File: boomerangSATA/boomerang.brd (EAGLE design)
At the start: 84.1 x 79.3 mm, 12 parts

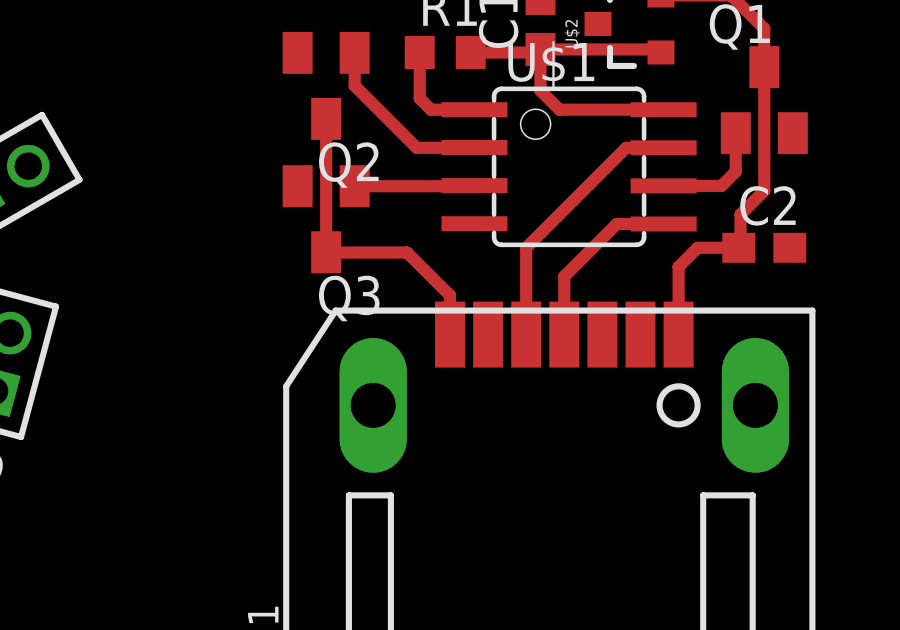
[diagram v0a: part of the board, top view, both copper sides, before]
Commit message: updated SATA - connector part in library used
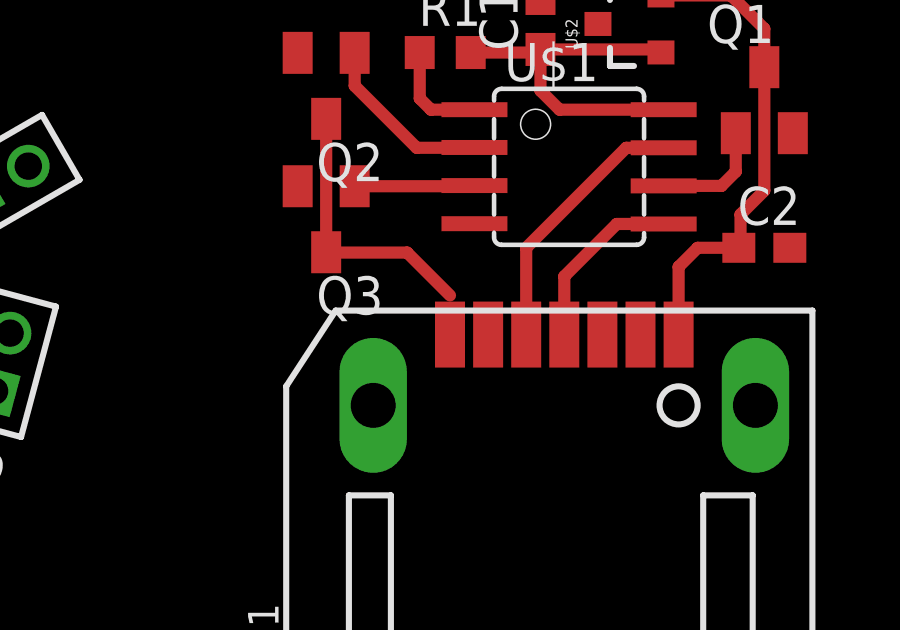
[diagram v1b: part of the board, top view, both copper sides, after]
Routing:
- net VCC: track 26.6 -> 25.3 mm
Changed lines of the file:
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@@
 <param name="tpViaShape" value="round"/>
 <param name="PrefDir.1" value="|"/>
-<param name="PrefDir.2" value="-"/>
-<param name="PrefDir.3" value="-"/>
-<param name="PrefDir.4" value="-"/>
-<param name="PrefDir.5" value="-"/>
-<param name="PrefDir.6" value="-"/>
-<param name="PrefDir.7" value="-"/>
-<param name="PrefDir.8" value="-"/>
+<param name="PrefDir.2" value="0"/>
+<param name="PrefDir.3" value="0"/>
+<param name="PrefDir.4" value="0"/>
+<param name="PrefDir.5" value="0"/>
+<param name="PrefDir.6" value="0"/>
+<param name="PrefDir.7" value="0"/>
+<param name="PrefDir.8" value="0"/>
 <param name="PrefDir.9" value="0"/>
 <param name="PrefDir.10" value="0"/>
 <param name="PrefDir.11" value="0"/>
-<param name="PrefDir.12" value="-"/>
-<param name="PrefDir.13" value="-"/>
-<param name="PrefDir.14" value="-"/>
-<param name="PrefDir.15" value="-"/>
+<param name="PrefDir.12" value="0"/>
+<param name="PrefDir.13" value="0"/>
+<param name="PrefDir.14" value="0"/>
+<param name="PrefDir.15" value="0"/>
 <param name="PrefDir.16" value="-"/>
 <param name="cfVia" value="8"/>
@@
 <contactref element="Q2" pad="3"/>
 <contactref element="Q1" pad="3"/>
-<contactref element="J1" pad="7"/>
 <wire x1="-3.81" y1="9.3775" x2="-3.81" y2="4.9325" width="0.4064" layer="1"/>
 <contactref element="J1" pad="1"/>
-<wire x1="0.3175" y1="2.1875" x2="0.3175" y2="3.4925" width="0.4064" layer="1"/>
 <wire x1="0.3175" y1="3.4925" x2="-1.11125" y2="4.92125" width="0.4064" layer="1"/>
 <wire x1="-1.11125" y1="4.92125" x2="-3.79875" y2="4.92125" width="0.4064" layer="1"/>
@@
 <wire x1="8.5725" y1="5.08" x2="7.9375" y2="4.445" width="0.4064" layer="1"/>
 <wire x1="7.9375" y1="4.445" x2="7.9375" y2="2.1875" width="0.4064" layer="1"/>
+<contactref element="J1" pad="7"/>
 <wire x1="0.3175" y1="2.1875" x2="7.9375" y2="2.1875" width="0" layer="19" extent="1-1"/>
+<wire x1="0.3175" y1="3.4925" x2="0.3175" y2="2.1875" width="0" layer="19" extent="1-1"/>
 </signal>
 <signal name="VCC_GOOD">

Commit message: foo
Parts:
- moved C-RO 21.3 mm to (14.4, -5.08), turned to 0 degrees
- moved C1 19.1 mm to (-0.16, -6.19)
- moved C2 19.1 mm to (7.30, -13.7)
- moved Q1 19.1 mm to (7.30, -8.73)
- moved Q2 19.1 mm to (-7.30, -8.26)
- moved U$2 19.1 mm to (2.86, -6.19)
- moved J1 19.1 mm to (0.64, -21.0)
- moved Q3 19.1 mm to (-7.30, -12.7)
- moved R1 19.1 mm to (-3.33, -7.14)
- moved U$1 19.1 mm to (0.79, -11.0)
- moved C-GO 15.3 mm to (0.32, 4.13), turned to 90 degrees
- moved C-BO 6.07 mm to (-14.0, -4.76), turned to 180 degrees
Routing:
- net GO: track 0.00 -> 17.2 mm
- net GND: track 0.00 -> 15.5 mm
- net BO: track 0.00 -> 8.86 mm
- net RO: track 0.00 -> 8.04 mm
- net VCC: track 25.3 -> 26.6 mm
- removed copper zone on layer 16, net GND
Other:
- board size 84.1 x 79.3 mm -> 89.8 x 80.4 mm
- board text added: "MUZY"
- board text removed: "BO"
- board text removed: "GO"
- board text removed: "RO"
